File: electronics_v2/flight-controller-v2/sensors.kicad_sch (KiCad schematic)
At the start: 12 parts

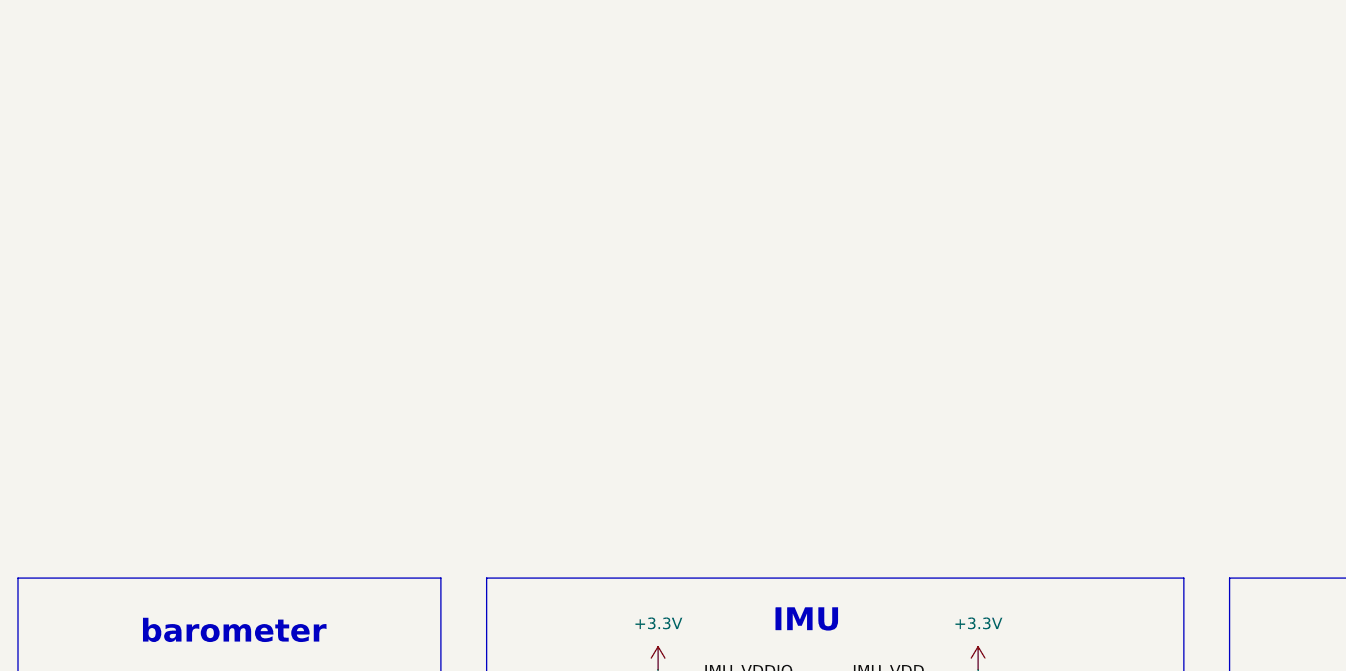
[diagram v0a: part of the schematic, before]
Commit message: develop Hall velocity sense circuit
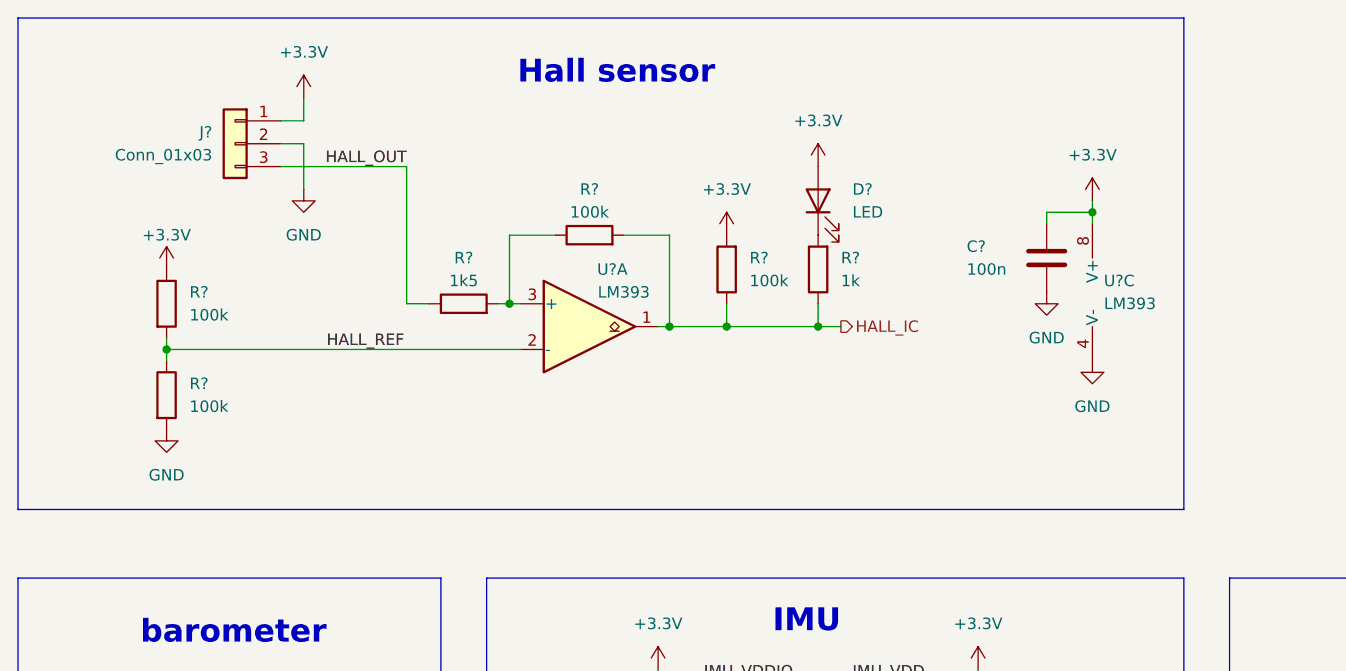
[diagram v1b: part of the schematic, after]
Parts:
- added C?: 100n, Capacitor_SMD:C_0603_1608Metric, symbol Device:C
- added D?: LED, LED_SMD:LED_0603_1608Metric, symbol Device:LED
- added J?: Conn_01x03, symbol Connector_Generic:Conn_01x03
- added R? (x3): 100k, symbol Device:R
- added R?: 1k, Resistor_SMD:R_0603_1608Metric, symbol Device:R
- added R?: 1k5, symbol Device:R
- added R?: 100k, Resistor_SMD:R_0603_1608Metric, symbol Device:R
- added U? (x2): LM393, symbol Comparator:LM393
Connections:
- net GND: now also C?.2, J?.2 (Pin_2), R?.2, U?.4 (V-)
- new net: R?.1, R?.2, U?.3 (+)
- new net: D?.1 (K), R?.2
- new net +3V3: C?.1, D?.2 (A), J?.1 (Pin_1), R?.1, R?.2, U?.8 (V+)
- new net HALL_IC: R?.1, R?.1, R?.2, U?.1
- new net HALL_OUT: J?.3 (Pin_3), R?.1
- new net HALL_REF: R?.1, R?.2, U?.2 (-)
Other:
- note added: "Hall sensor"

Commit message: FC scheme complete
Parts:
- removed J?: Conn_01x03, symbol Connector_Generic:Conn_01x03
- added U4: CS49E, goose:tht_pin_01x03, symbol goose:CS49E
- R20, R23, R24, R25: renamed from R?; footprint (none) -> Resistor_SMD:R_0603_1608Metric
- U5: renamed from U?; footprint (none) -> Package_SO:SOIC-8_3.9x4.9mm_P1.27mm
- gave numbers to parts that had none: 16
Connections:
- net +3V3: now also U4.1 (VCC)
- net GND: now also U4.2 (GND)
- net HALL_OUT: now also U4.3 (VOUT)
- net HALL_IC renamed HALL
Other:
- moved on the sheet: C22, D6, R20, R21, R22, R23, R24, R25, U5A, U5C

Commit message: first board cutout and layout
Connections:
- net COMP_P: now reaches R20.1, R24.2, U5.3 (+)
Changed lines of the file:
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@@
     (effects (font (size 1.27 1.27)) (justify left bottom))
+  )
+  (label "COMP_P" (at 184.15 49.53 180)
+    (effects (font (size 1.27 1.27)) (justify right bottom))
   )
   (label "MAG_C1" (at 224.79 128.27 0)

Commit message: edge XT60 connector & INA226 I2C measurement
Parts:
- added J6: Conn_02x03_Odd_Even, Connector_IDC:IDC-Header_2x03_P2.54mm_Vertical, symbol Connector_Generic:Conn_02x03_Odd_Even
- renumbered C26 to C19, C27 to C20, C23 to C21, C24 to C22, C30 to C23, C31 to C24, C29 to C25, C25 to C26, C22 to C27, D6 to D4, R23 to R16, R25 to R17, R24 to R18, R20 to R19, R21 to R20, R22 to R21, U8 to U4, U4 to U5, U5 to U7, U7 to U8
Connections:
- net +3.3V: now also J6.6 (Pin_6)
- net GND: now also J6.5 (Pin_5)
- net I2C_SCL renamed INT_I2C_SCL
- net I2C_SDA renamed INT_I2C_SDA
- new net EXT_I2C3_SCL: J6.4 (Pin_4)
- new net EXT_I2C3_SDA: J6.3 (Pin_3)
- new net VLX_INT: J6.2 (Pin_2)
- new net VLX_XSHUT: J6.1 (Pin_1)
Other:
- note added: "I2C address: 0x52"
- note added: "TOF sensor"

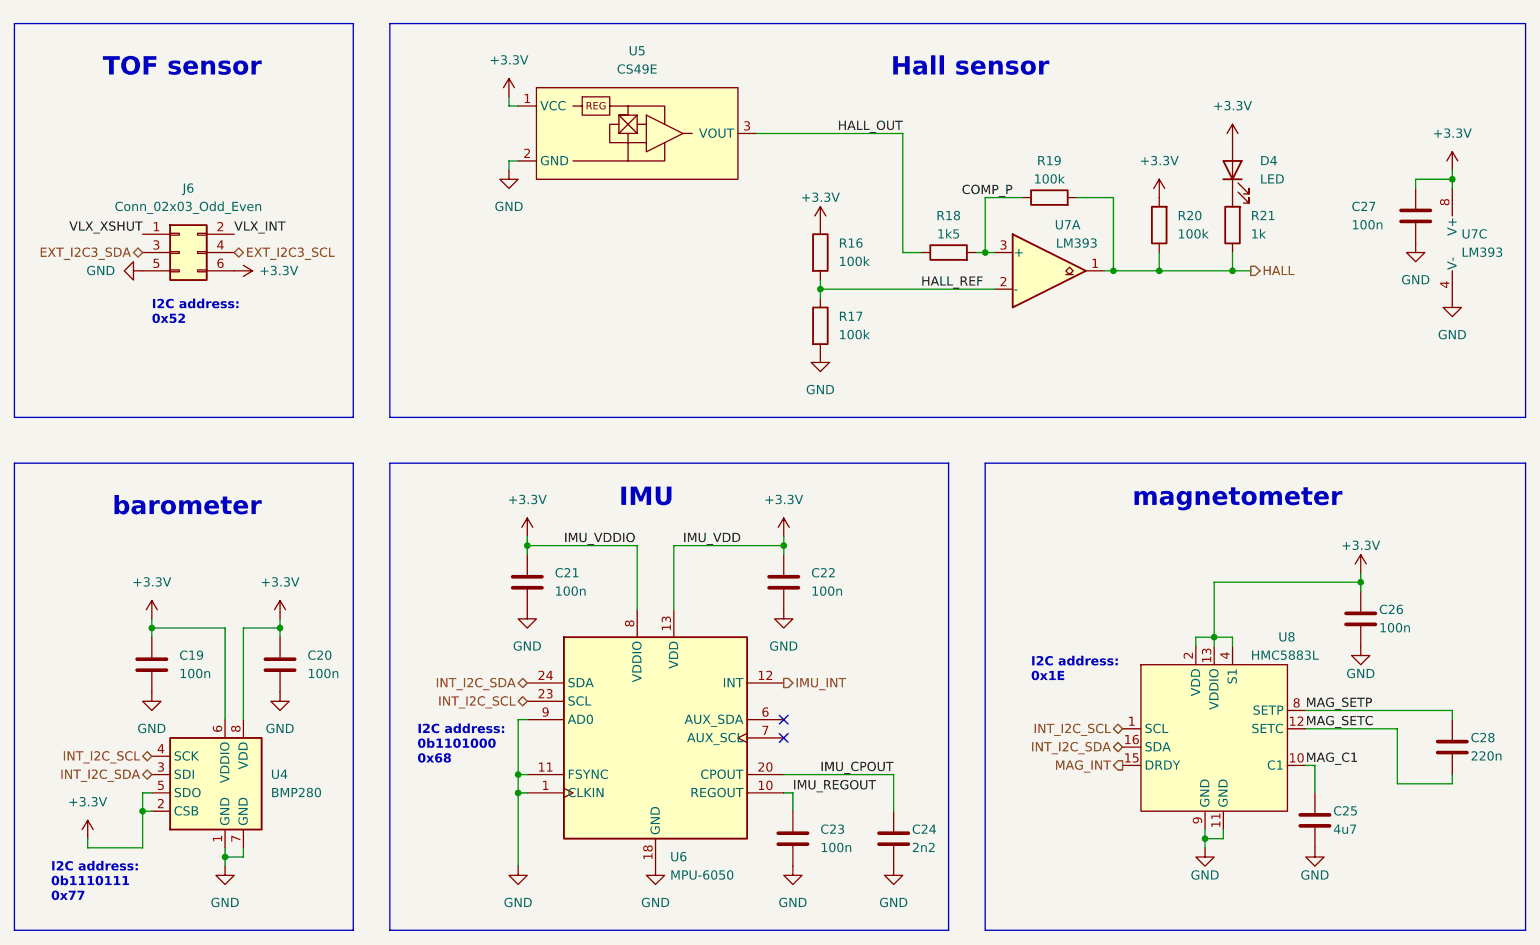
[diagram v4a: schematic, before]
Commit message: move PLI to FC
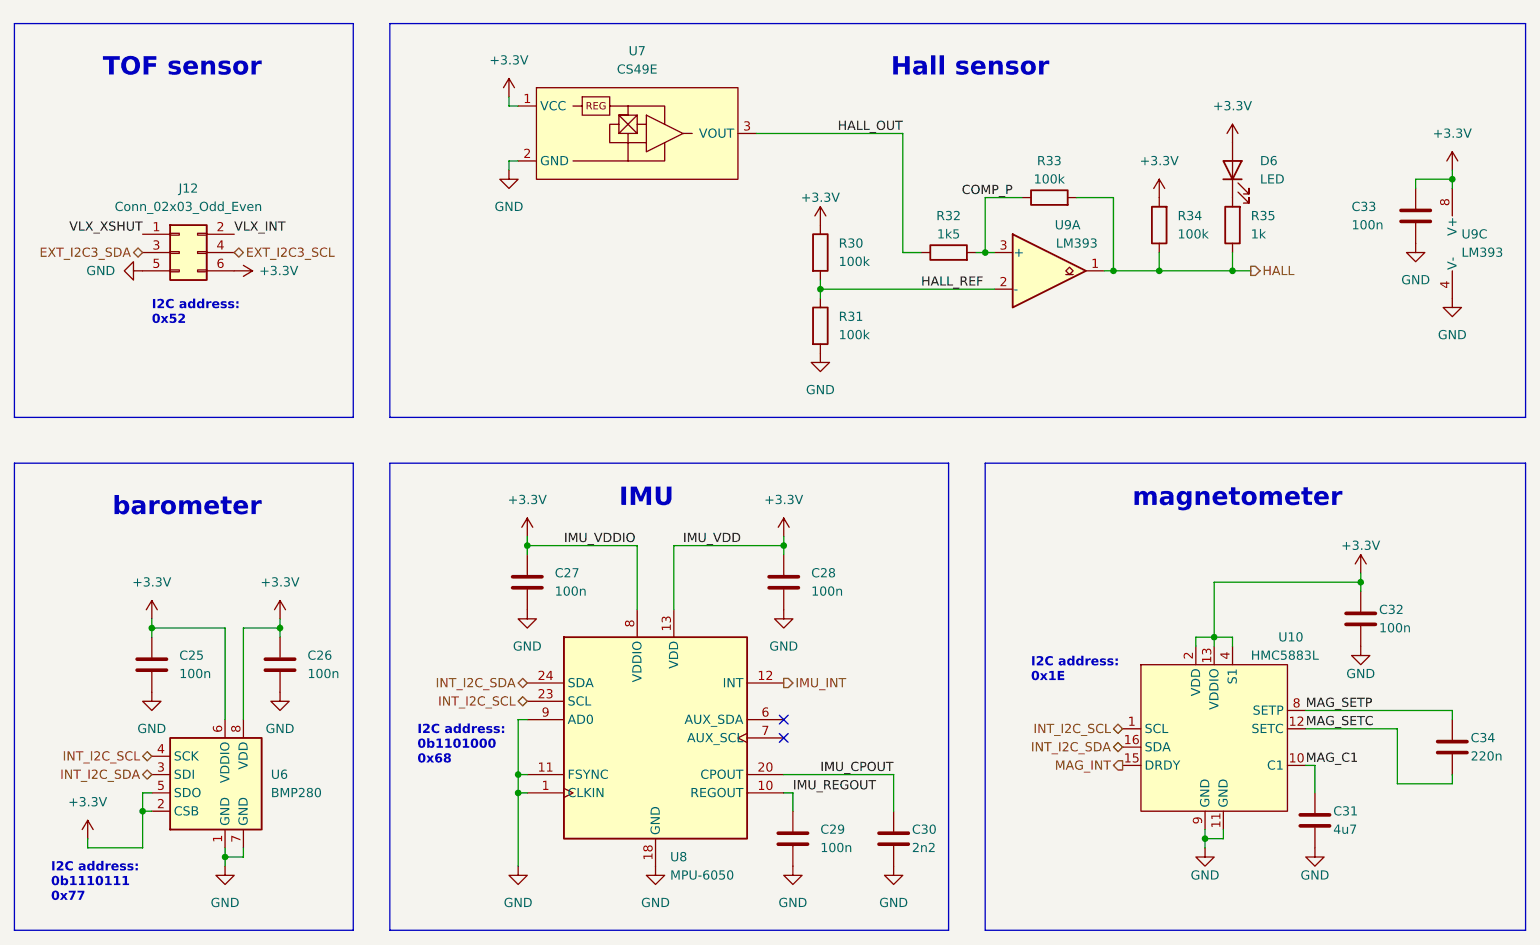
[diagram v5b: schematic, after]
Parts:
- renumbered C19 to C25, C20 to C26, C21 to C27, C22 to C28, C23 to C29, C24 to C30, C25 to C31, C26 to C32, C27 to C33, C28 to C34, D4 to D6, J6 to J12, R16 to R30, R17 to R31, R18 to R32, R19 to R33, R20 to R34, R21 to R35, U8 to U10, U4 to U6, U5 to U7, U6 to U8, U7 to U9

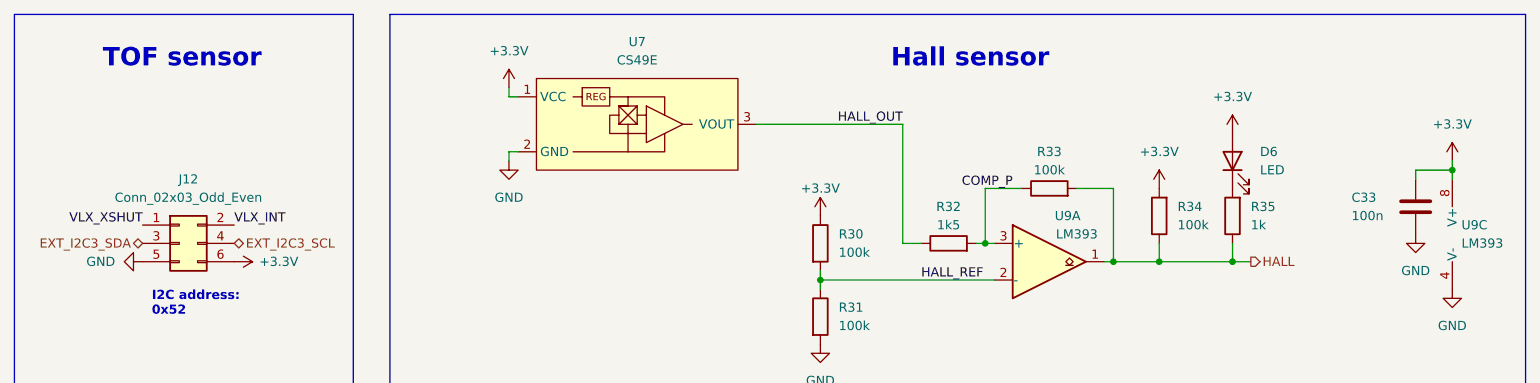
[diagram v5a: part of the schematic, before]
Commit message: fix route names
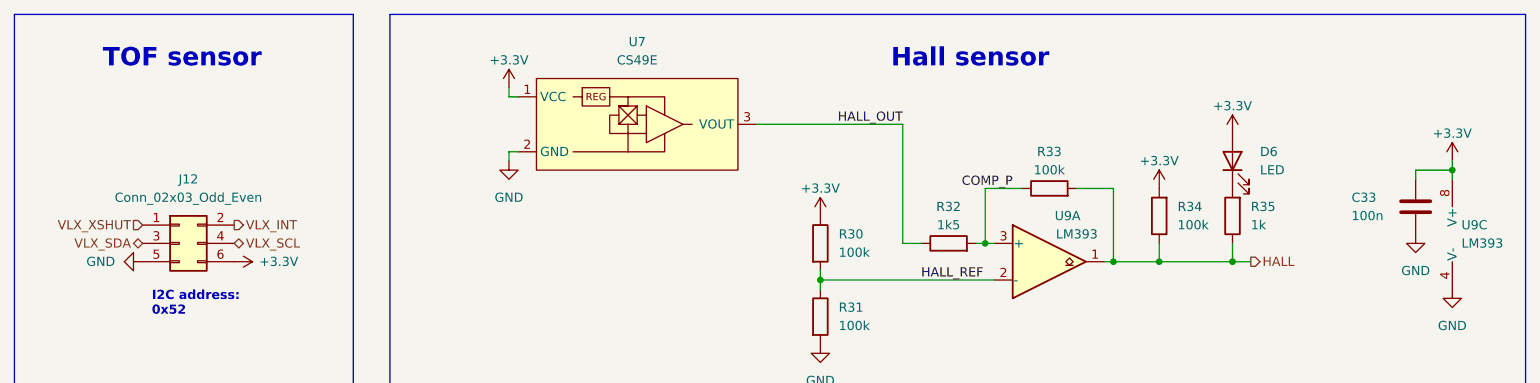
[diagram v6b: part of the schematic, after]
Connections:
- net +3V3 is gone; now on net +3.3V: C33.1, D6.2 (A), R30.1, R34.2, U7.1 (VCC), U9.8 (V+)
- net EXT_I2C3_SCL renamed VLX_SCL
- net EXT_I2C3_SDA renamed VLX_SDA
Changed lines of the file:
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@@
-    (effects (font (size 1.27 1.27)) (justify left bottom))
-  )
-  (label "VLX_XSHUT" (at 63.5 54.61 180)
-    (effects (font (size 1.27 1.27)) (justify right bottom))
-  )
-  (label "VLX_INT" (at 76.2 54.61 0)
     (effects (font (size 1.27 1.27)) (justify left bottom))
   )
@@
     (effects (font (size 1.27 1.27)) (justify right))
   )
-  (hierarchical_label "EXT_I2C3_SCL" (shape bidirectional) (at 76.2 57.15 0)
+  (hierarchical_label "VLX_SCL" (shape bidirectional) (at 76.2 57.15 0)
     (effects (font (size 1.27 1.27)) (justify left))
   )
@@
     (effects (font (size 1.27 1.27)) (justify right))
   )
+  (hierarchical_label "VLX_XSHUT" (shape input) (at 63.5 54.61 180)
+    (effects (font (size 1.27 1.27)) (justify right))
+  )
   (hierarchical_label "INT_I2C_SCL" (shape bidirectional) (at 199.39 123.19 180)
     (effects (font (size 1.27 1.27)) (justify right))
   )
-  (hierarchical_label "EXT_I2C3_SDA" (shape bidirectional) (at 63.5 57.15 180)
+  (hierarchical_label "VLX_INT" (shape output) (at 76.2 54.61 0)
+    (effects (font (size 1.27 1.27)) (justify left))
+  )
+  (hierarchical_label "VLX_SDA" (shape bidirectional) (at 63.5 57.15 180)
     (effects (font (size 1.27 1.27)) (justify right))
   )
@@
     (pin "2")
   )
-  (symbol (lib_name "+3.3V_1") (lib_id "power:+3.3V") (at 114.3 35.56 0) (mirror y) (unit 1)
-    (in_bom yes) (on_board yes) (fields_autoplaced)
-    (property "Reference" "#PWR080" (id 0) (at 114.3 39.37 0)
-      (effects (font (size 1.27 1.27)) hide)
-    )
-    (property "Value" "+3.3V" (id 1) (at 114.3 30.48 0))
-    (property "Footprint" "" (id 2) (at 114.3 35.56 0)
-      (effects (font (size 1.27 1.27)) hide)
-    )
-    (property "Datasheet" "" (id 3) (at 114.3 35.56 0)
-      (effects (font (size 1.27 1.27)) hide)
-    )
-    (pin "1")
-  )
-  (symbol (lib_name "+3.3V_1") (lib_id "power:+3.3V") (at 204.47 49.53 0) (mirror y) (unit 1)
-    (in_bom yes) (on_board yes) (fields_autoplaced)
-    (property "Reference" "#PWR092" (id 0) (at 204.47 53.34 0)
-      (effects (font (size 1.27 1.27)) hide)
-    )
-    (property "Value" "+3.3V" (id 1) (at 204.47 44.45 0))
+  (symbol (lib_id "power:+3.3V") (at 245.11 45.72 0) (unit 1)
+    (in_bom yes) (on_board yes)
+    (property "Reference" "#PWR0101" (id 0) (at 245.11 49.53 0)
+      (effects (font (size 1.27 1.27)) hide)
+    )
+    (property "Value" "+3.3V" (id 1) (at 245.11 41.91 0))
+    (property "Footprint" "" (id 2) (at 245.11 45.72 0)
+      (effects (font (size 1.27 1.27)) hide)
+    )
+    (property "Datasheet" "" (id 3) (at 245.11 45.72 0)
+      (effects (font (size 1.27 1.27)) hide)
+    )
+    (pin "1")
+  )
+  (symbol (lib_id "power:+3.3V") (at 204.47 49.53 0) (unit 1)
+    (in_bom yes) (on_board yes)
+    (property "Reference" "#PWR0102" (id 0) (at 204.47 53.34 0)
+      (effects (font (size 1.27 1.27)) hide)
+    )
+    (property "Value" "+3.3V" (id 1) (at 204.47 45.72 0))
     (property "Footprint" "" (id 2) (at 204.47 49.53 0)
       (effects (font (size 1.27 1.27)) hide)
@@
     (pin "2")
   )
-  (symbol (lib_name "+3.3V_1") (lib_id "power:+3.3V") (at 214.63 41.91 0) (mirror y) (unit 1)
-    (in_bom yes) (on_board yes) (fields_autoplaced)
-    (property "Reference" "#PWR094" (id 0) (at 214.63 45.72 0)
-      (effects (font (size 1.27 1.27)) hide)
-    )
-    (property "Value" "+3.3V" (id 1) (at 214.63 36.83 0))
-    (property "Footprint" "" (id 2) (at 214.63 41.91 0)
-      (effects (font (size 1.27 1.27)) hide)
-    )
-    (property "Datasheet" "" (id 3) (at 214.63 41.91 0)
-      (effects (font (size 1.27 1.27)) hide)
-    )
-    (pin "1")
-  )
   (symbol (lib_id "power:+3.3V") (at 64.77 107.95 0) (unit 1)
     (in_bom yes) (on_board yes) (fields_autoplaced)
@@
     (pin "3")
   )
-  (symbol (lib_name "+3.3V_1") (lib_id "power:+3.3V") (at 245.11 45.72 0) (unit 1)
-    (in_bom yes) (on_board yes) (fields_autoplaced)
-    (property "Reference" "#PWR099" (id 0) (at 245.11 49.53 0)
-      (effects (font (size 1.27 1.27)) hide)
-    )
-    (property "Value" "+3.3V" (id 1) (at 245.11 40.64 0))
-    (property "Footprint" "" (id 2) (at 245.11 45.72 0)
-      (effects (font (size 1.27 1.27)) hide)
-    )
-    (property "Datasheet" "" (id 3) (at 245.11 45.72 0)
-      (effects (font (size 1.27 1.27)) hide)
-    )
-    (pin "1")
-  )
   (symbol (lib_id "power:GND") (at 114.3 45.72 0) (mirror y) (unit 1)
     (in_bom yes) (on_board yes)
@@
     (pin "1")
     (pin "2")
+  )
+  (symbol (lib_id "power:+3.3V") (at 114.3 35.56 0) (unit 1)
+    (in_bom yes) (on_board yes)
+    (property "Reference" "#PWR0105" (id 0) (at 114.3 39.37 0)
+      (effects (font (size 1.27 1.27)) hide)
+    )
+    (property "Value" "+3.3V" (id 1) (at 114.3 31.75 0))
+    (property "Footprint" "" (id 2) (at 114.3 35.56 0)
+      (effects (font (size 1.27 1.27)) hide)
+    )
+    (property "Datasheet" "" (id 3) (at 114.3 35.56 0)
+      (effects (font (size 1.27 1.27)) hide)
+    )
+    (pin "1")
   )
   (symbol (lib_id "power:GND") (at 134.62 142.24 0) (unit 1)
@@
     (pin "1")
   )
+  (symbol (lib_id "power:+3.3V") (at 214.63 41.91 0) (unit 1)
+    (in_bom yes) (on_board yes)
+    (property "Reference" "#PWR0103" (id 0) (at 214.63 45.72 0)
+      (effects (font (size 1.27 1.27)) hide)
+    )
+    (property "Value" "+3.3V" (id 1) (at 214.63 38.1 0))
+    (property "Footprint" "" (id 2) (at 214.63 41.91 0)
+      (effects (font (size 1.27 1.27)) hide)
+    )
+    (property "Datasheet" "" (id 3) (at 214.63 41.91 0)
+      (effects (font (size 1.27 1.27)) hide)
+    )
+    (pin "1")
+  )
   (symbol (lib_id "Connector_Generic:Conn_02x03_Odd_Even") (at 68.58 57.15 0) (unit 1)
     (in_bom yes) (on_board yes) (fields_autoplaced)
@@
     )
     (property "Datasheet" "" (id 3) (at 55.88 138.43 0)
-      (effects (font (size 1.27 1.27)) hide)
-    )
-    (pin "1")
-  )
-  (symbol (lib_name "+3.3V_1") (lib_id "power:+3.3V") (at 157.48 53.34 0) (mirror y) (unit 1)
-    (in_bom yes) (on_board yes)
-    (property "Reference" "#PWR089" (id 0) (at 157.48 57.15 0)
-      (effects (font (size 1.27 1.27)) hide)
-    )
-    (property "Value" "+3.3V" (id 1) (at 157.48 49.53 0))
-    (property "Footprint" "" (id 2) (at 157.48 53.34 0)
-      (effects (font (size 1.27 1.27)) hide)
-    )
-    (property "Datasheet" "" (id 3) (at 157.48 53.34 0)
       (effects (font (size 1.27 1.27)) hide)
     )
@@
     (pin "9")
   )
+  (symbol (lib_id "power:+3.3V") (at 157.48 53.34 0) (unit 1)
+    (in_bom yes) (on_board yes)
+    (property "Reference" "#PWR0104" (id 0) (at 157.48 57.15 0)
+      (effects (font (size 1.27 1.27)) hide)
+    )
+    (property "Value" "+3.3V" (id 1) (at 157.48 49.53 0))
+    (property "Footprint" "" (id 2) (at 157.48 53.34 0)
+      (effects (font (size 1.27 1.27)) hide)
+    )
+    (property "Datasheet" "" (id 3) (at 157.48 53.34 0)
+      (effects (font (size 1.27 1.27)) hide)
+    )
+    (pin "1")
+  )
   (symbol (lib_id "power:GND") (at 240.03 55.88 0) (unit 1)
